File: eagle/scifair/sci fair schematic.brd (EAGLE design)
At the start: 34 x 58.4 mm, 12 parts, among them IC1 LM555N, Q1 BC817-16W, Q2 BC817-16W, Q3 BC817-16W, X1 RIGHT, X2 LEFT, X3 PWR

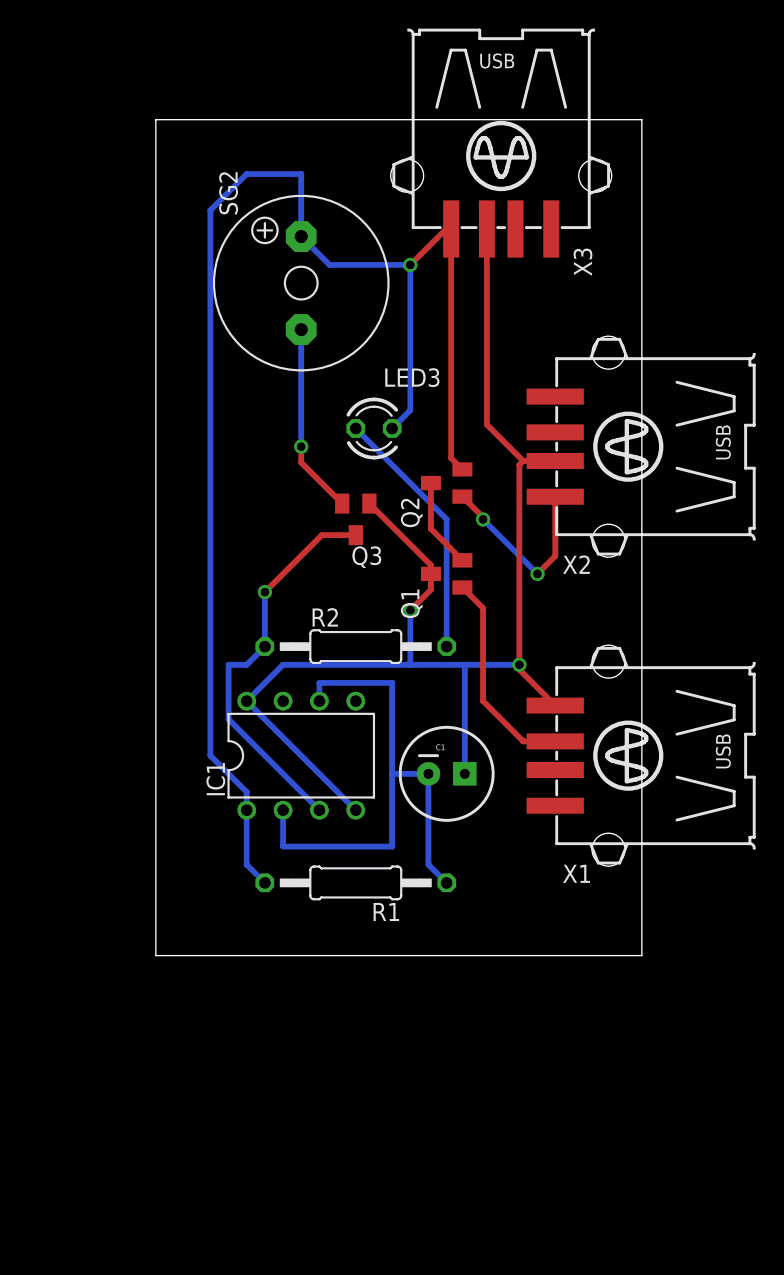
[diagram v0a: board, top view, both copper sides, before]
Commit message: Rework design in entirety to solve issues with previous design
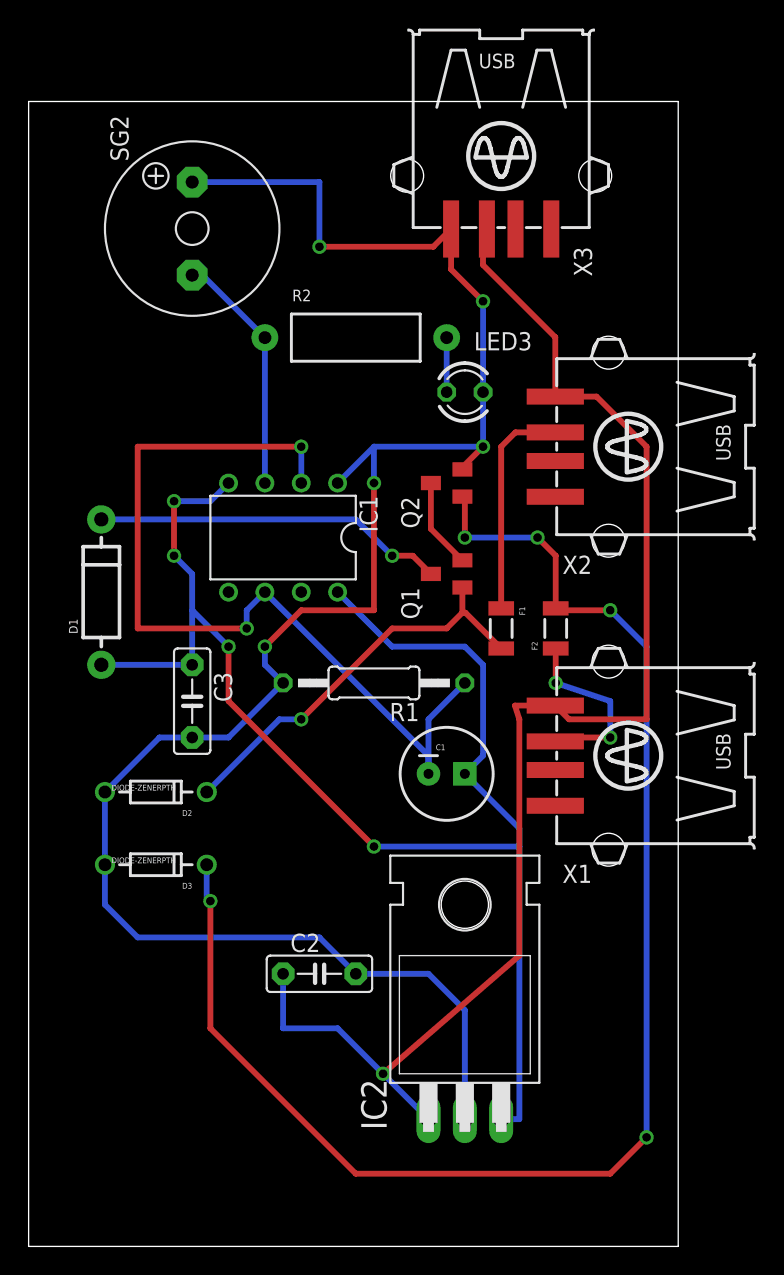
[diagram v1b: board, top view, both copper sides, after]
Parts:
- removed Q3: BC817-16W, semicon-smd-ipc:SOT23
- added C2, C3: (no value), capacitor-wima:C5B2.5
- added D1: (no value), SparkFun-DiscreteSemi:DIODE-1N4001
- added D2, D3: DIODE-ZENERPTH, SparkFun-DiscreteSemi:DIODE-ZENER
- added F1, F2: PTCSMD, SparkFun-PowerIC:PTC-1206
- added IC2: LM340H-12, linear:TO220H
- R2: device rcl:0207/12 -> SparkFun-Passives:AXIAL-0.5
- moved R2 21.6 mm to (80.0, 64.8)
- moved IC1 15.3 mm to (74.9, 50.8), turned to 180 degrees
- moved R1 14.0 mm to (81.3, 40.6)
- moved SG2 8.52 mm to (68.6, 72.4)
- moved LED3 6.84 mm to (87.6, 61.0)
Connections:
- new net N$1: C2.1, IC2.1, X1.4, X2.4, X3.3
- new net N$12: LED3.A, R2.P$2
- new net N$5: C2.2, C3.2, D2.P$2, D3.P$2, IC1.1, IC2.2, LED3.K, Q2.2, R1.2, SG2.+, X3.4
- net N$10: now also IC1.3, R2.P$1, SG2.-; no longer LED3.A, R2.2
- net N$2: now also F1.1, X2.3; no longer Q1.1, X1.3
- net N$3: now also F2.1, X1.3; no longer Q2.1, X2.1
- net N$6: now also C1.1, C3.1, D1.A, IC1.4, IC1.8, IC2.3; no longer Q3.2, SG2.-
- net N$7: now also D1.C, Q1.3; no longer IC1.1, LED3.K, Q2.2, R1.2, SG2.+, X3.4
- net N$8: now also D2.P$1, F1.2, Q1.1; no longer C1.1, IC1.4, IC1.8, Q1.3, Q3.1, X1.4, X2.2, X3.3
- net N$9: now also D3.P$1, F2.2, Q2.1; no longer IC1.3, Q3.3, R2.1
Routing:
- net N$5: track 0.00 -> 135.1 mm, vias 0 -> 5
- net N$1: track 0.00 -> 97.1 mm, vias 0 -> 1
- net N$6: track 13.3 -> 102.0 mm, vias 1 -> 4
- net N$7: track 101.8 -> 24.6 mm
- net N$9: track 27.7 -> 102.5 mm, vias 1 -> 5
- net N$8: track 90.3 -> 28.6 mm, vias 2 -> 1
- net N$11: track 38.6 -> 62.2 mm, vias 0 -> 2
- net N$12: track 0.00 -> 3.81 mm
- net N$10: track 17.9 -> 17.0 mm
- net N$2: track 14.8 -> 15.5 mm
- net N$3: track 13.5 -> 12.9 mm
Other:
- board size 34 x 58.4 mm -> 45.4 x 80 mm

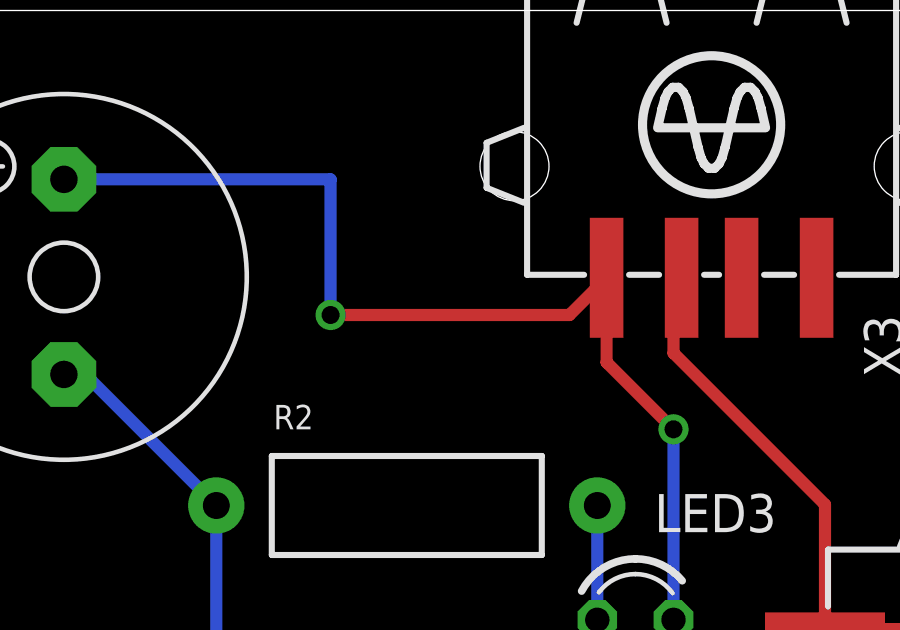
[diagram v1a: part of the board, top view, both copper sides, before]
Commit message: Add a space using vias for jumpers to go to a rocker switch
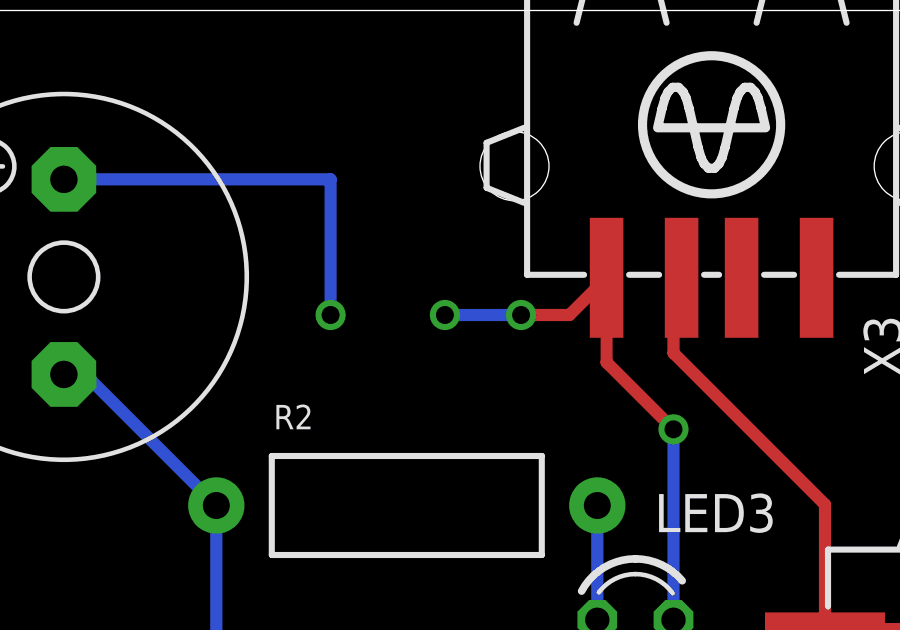
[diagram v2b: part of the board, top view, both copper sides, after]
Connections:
- net N$5 renamed GND
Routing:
- net GND: track 135.1 -> 131.3 mm, vias 5 -> 7
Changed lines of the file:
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@@
 <layer number="99" name="SpiceOrder" color="5" fill="1" visible="no" active="no"/>
 <layer number="100" name="Muster" color="7" fill="1" visible="no" active="no"/>
-<layer number="101" name="Patch_Top" color="12" fill="4" visible="no" active="yes"/>
-<layer number="102" name="Vscore" color="7" fill="1" visible="no" active="yes"/>
-<layer number="103" name="tMap" color="7" fill="1" visible="no" active="yes"/>
-<layer number="104" name="Name" color="16" fill="1" visible="no" active="yes"/>
-<layer number="105" name="tPlate" color="7" fill="1" visible="no" active="yes"/>
-<layer number="106" name="bPlate" color="7" fill="1" visible="no" active="yes"/>
-<layer number="107" name="Crop" color="7" fill="1" visible="no" active="yes"/>
+<layer number="101" name="Patch_Top" color="12" fill="4" visible="yes" active="yes"/>
+<layer number="102" name="Vscore" color="7" fill="1" visible="yes" active="yes"/>
+<layer number="103" name="tMap" color="7" fill="1" visible="yes" active="yes"/>
+<layer number="104" name="Name" color="16" fill="1" visible="yes" active="yes"/>
+<layer number="105" name="tPlate" color="7" fill="1" visible="yes" active="yes"/>
+<layer number="106" name="bPlate" color="7" fill="1" visible="yes" active="yes"/>
+<layer number="107" name="Crop" color="7" fill="1" visible="yes" active="yes"/>
 <layer number="108" name="tplace-old" color="10" fill="1" visible="yes" active="yes"/>
 <layer number="109" name="ref-old" color="11" fill="1" visible="yes" active="yes"/>
@@
 <layer number="112" name="tSilk" color="7" fill="1" visible="yes" active="yes"/>
 <layer number="113" name="IDFDebug" color="7" fill="1" visible="yes" active="yes"/>
-<layer number="116" name="Patch_BOT" color="9" fill="4" visible="no" active="yes"/>
+<layer number="116" name="Patch_BOT" color="9" fill="4" visible="yes" active="yes"/>
 <layer number="118" name="Rect_Pads" color="7" fill="1" visible="yes" active="yes"/>
-<layer number="121" name="_tsilk" color="7" fill="1" visible="no" active="yes"/>
-<layer number="122" name="_bsilk" color="7" fill="1" visible="no" active="yes"/>
+<layer number="121" name="_tsilk" color="7" fill="1" visible="yes" active="yes"/>
+<layer number="122" name="_bsilk" color="7" fill="1" visible="yes" active="yes"/>
 <layer number="123" name="tTestmark" color="7" fill="1" visible="yes" active="yes"/>
 <layer number="124" name="bTestmark" color="7" fill="1" visible="yes" active="yes"/>
-<layer number="125" name="_tNames" color="7" fill="1" visible="no" active="yes"/>
+<layer number="125" name="_tNames" color="7" fill="1" visible="yes" active="yes"/>
 <layer number="126" name="_bNames" color="7" fill="1" visible="yes" active="yes"/>
 <layer number="127" name="_tValues" color="7" fill="1" visible="yes" active="yes"/>
@@
 <layer number="131" name="tAdjust" color="7" fill="1" visible="yes" active="yes"/>
 <layer number="132" name="bAdjust" color="7" fill="1" visible="yes" active="yes"/>
-<layer number="144" name="Drill_legend" color="7" fill="1" visible="no" active="yes"/>
+<layer number="144" name="Drill_legend" color="7" fill="1" visible="yes" active="yes"/>
 <layer number="150" name="Notes" color="7" fill="1" visible="yes" active="yes"/>
-<layer number="151" name="HeatSink" color="7" fill="1" visible="no" active="yes"/>
+<layer number="151" name="HeatSink" color="7" fill="1" visible="yes" active="yes"/>
 <layer number="152" name="_bDocu" color="7" fill="1" visible="yes" active="yes"/>
 <layer number="153" name="FabDoc1" color="7" fill="1" visible="yes" active="yes"/>
@@
 <layer number="155" name="FabDoc3" color="7" fill="1" visible="yes" active="yes"/>
 <layer number="199" name="Contour" color="7" fill="1" visible="yes" active="yes"/>
-<layer number="200" name="200bmp" color="1" fill="10" visible="no" active="yes"/>
-<layer number="201" name="201bmp" color="2" fill="10" visible="no" active="yes"/>
-<layer number="202" name="202bmp" color="3" fill="10" visible="no" active="yes"/>
-<layer number="203" name="203bmp" color="4" fill="10" visible="no" active="yes"/>
-<layer number="204" name="204bmp" color="5" fill="10" visible="no" active="yes"/>
-<layer number="205" name="205bmp" color="6" fill="10" visible="no" active="yes"/>
-<layer number="206" name="206bmp" color="7" fill="10" visible="no" active="yes"/>
-<layer number="207" name="207bmp" color="8" fill="10" visible="no" active="yes"/>
-<layer number="208" name="208bmp" color="9" fill="10" visible="no" active="yes"/>
-<layer number="209" name="209bmp" color="7" fill="1" visible="no" active="yes"/>
-<layer number="210" name="210bmp" color="7" fill="1" visible="no" active="yes"/>
-<layer number="211" name="211bmp" color="7" fill="1" visible="no" active="yes"/>
-<layer number="212" name="212bmp" color="7" fill="1" visible="no" active="yes"/>
-<layer number="213" name="213bmp" color="7" fill="1" visible="no" active="yes"/>
-<layer number="214" name="214bmp" color="7" fill="1" visible="no" active="yes"/>
-<layer number="215" name="215bmp" color="7" fill="1" visible="no" active="yes"/>
-<layer number="216" name="216bmp" color="7" fill="1" visible="no" active="yes"/>
+<layer number="200" name="200bmp" color="1" fill="10" visible="yes" active="yes"/>
+<layer number="201" name="201bmp" color="2" fill="10" visible="yes" active="yes"/>
+<layer number="202" name="202bmp" color="3" fill="10" visible="yes" active="yes"/>
+<layer number="203" name="203bmp" color="4" fill="10" visible="yes" active="yes"/>
+<layer number="204" name="204bmp" color="5" fill="10" visible="yes" active="yes"/>
+<layer number="205" name="205bmp" color="6" fill="10" visible="yes" active="yes"/>
+<layer number="206" name="206bmp" color="7" fill="10" visible="yes" active="yes"/>
+<layer number="207" name="207bmp" color="8" fill="10" visible="yes" active="yes"/>
+<layer number="208" name="208bmp" color="9" fill="10" visible="yes" active="yes"/>
+<layer number="209" name="209bmp" color="7" fill="1" visible="yes" active="yes"/>
+<layer number="210" name="210bmp" color="7" fill="1" visible="yes" active="yes"/>
+<layer number="211" name="211bmp" color="7" fill="1" visible="yes" active="yes"/>
+<layer number="212" name="212bmp" color="7" fill="1" visible="yes" active="yes"/>
+<layer number="213" name="213bmp" color="7" fill="1" visible="yes" active="yes"/>
+<layer number="214" name="214bmp" color="7" fill="1" visible="yes" active="yes"/>
+<layer number="215" name="215bmp" color="7" fill="1" visible="yes" active="yes"/>
+<layer number="216" name="216bmp" color="7" fill="1" visible="yes" active="yes"/>
 <layer number="217" name="217bmp" color="18" fill="1" visible="no" active="no"/>
 <layer number="218" name="218bmp" color="19" fill="1" visible="no" active="no"/>
@@
 <layer number="250" name="Descript" color="3" fill="1" visible="no" active="no"/>
 <layer number="251" name="SMDround" color="12" fill="11" visible="no" active="no"/>
-<layer number="254" name="cooling" color="7" fill="1" visible="no" active="yes"/>
+<layer number="254" name="cooling" color="7" fill="1" visible="yes" active="yes"/>
 <layer number="255" name="routoute" color="7" fill="1" visible="yes" active="yes"/>
 </layers>
@@
 <wire x1="85.26" y1="51.41" x2="87.46" y2="49.21" width="0.4064" layer="1"/>
 </signal>
-<signal name="N$5">
+<signal name="GND">
 <contactref element="X3" pad="4"/>
 <contactref element="IC2" pad="2"/>
@@
 <wire x1="77.47" y1="75.6412" x2="77.47" y2="71.12" width="0.4064" layer="16"/>
 <via x="77.47" y="71.12" extent="1-16" drill="0.6" shape="square"/>
-<wire x1="77.47" y1="71.12" x2="85.43" y2="71.12" width="0.4064" layer="1"/>
 <wire x1="85.43" y1="71.12" x2="86.67" y2="72.36" width="0.4064" layer="1"/>
 <wire x1="68.58" y1="36.83" x2="66.294" y2="36.83" width="0.4064" layer="16"/>
@@
 <via x="81.28" y="54.61" extent="1-16" drill="0.6" shape="square"/>
 <wire x1="81.28" y1="54.61" x2="81.28" y2="57.15" width="0.4064" layer="16"/>
+<via x="81.28" y="71.12" extent="1-16" drill="0.6" shape="square"/>
+<wire x1="81.28" y1="71.12" x2="77.47" y2="71.12" width="0" layer="19" extent="1-1"/>
+<wire x1="81.28" y1="71.12" x2="83.82" y2="71.12" width="0.4064" layer="16"/>
+<via x="83.82" y="71.12" extent="1-16" drill="0.6" shape="square"/>
+<wire x1="83.82" y1="71.12" x2="85.43" y2="71.12" width="0.4064" layer="1"/>
 </signal>
 <signal name="N$6">
